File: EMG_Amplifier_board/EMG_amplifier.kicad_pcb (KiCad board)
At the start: 2 copper layers, 50 x 28 mm, 53 parts, among them J1 Conn_01x04_Socket, J2 Conn_01x04_Pin, J3 Conn_01x06_Pin, J4 Conn_01x06_Socket, J7 Conn_01x06_Pin, U1 LPV821DBVR, U2 INA333xxDGK, U3 LPV821DBVR, U5 LPV821DBVR, U6 LPV821DBVR, U7 TPD2E001DRLR, U8 TLV8542DR

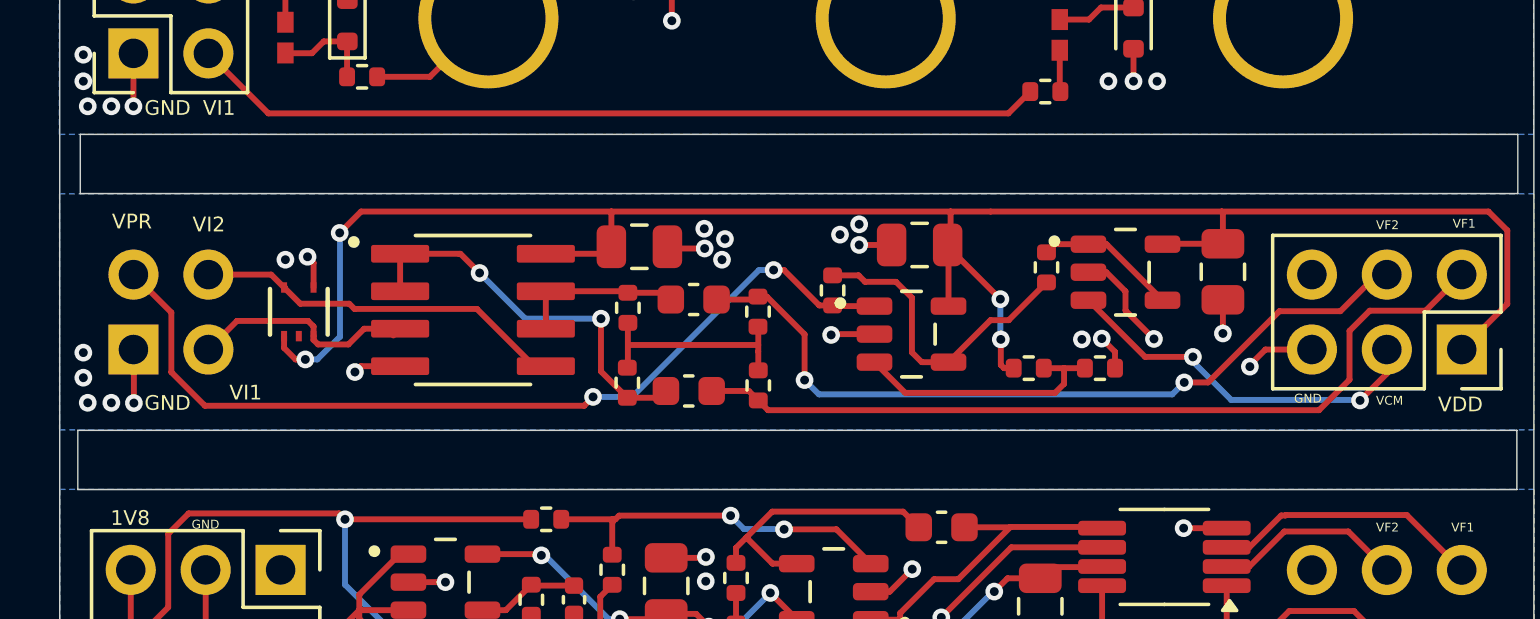
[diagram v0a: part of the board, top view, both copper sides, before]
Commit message: add capacitor to ESD
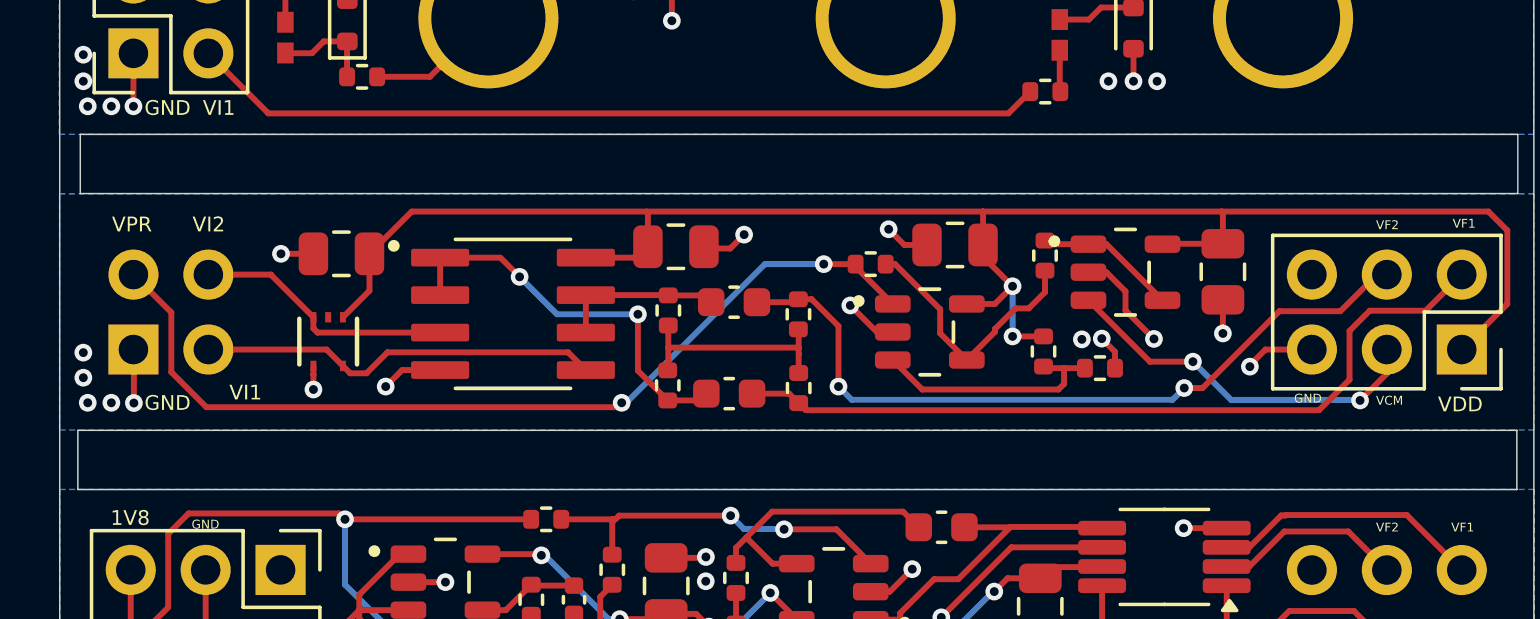
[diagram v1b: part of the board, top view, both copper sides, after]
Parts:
- added C12: 0.1uF, Capacitor_SMD:C_0805_2012Metric, F.Cu at (21.6, 24.1)
- E1: value E1 -> E
- E3: value E2 -> E
- moved R16 1.57 mm to (39.5, 24.4), turned to 180 degrees
- moved U7 1.42 mm to (21.1, 27.0), turned to -90 degrees
- moved R6 1.37 mm to (32.6, 28.5)
- moved R7 1.37 mm to (32.6, 26.0)
- moved C1 1.37 mm to (34.7, 28.8)
- moved C2 1.37 mm to (34.9, 25.7)
- moved R8 1.37 mm to (37.0, 28.6)
- moved R9 1.37 mm to (37.0, 26.1)
- moved U8 1.36 mm to (27.4, 26.1)
- moved C7 1.24 mm to (32.9, 23.8)
- moved C9 1.20 mm to (42.4, 23.8)
- moved R23 0.76 mm to (45.4, 27.4), turned to -90 degrees
- moved U6 0.62 mm to (41.5, 26.7)
- moved R15 0.40 mm to (45.4, 24.1)
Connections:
- J1 pad 2: /Electrode_Board/V_I1 -> /Electrode_Board/V_I2
- J1 pad 4: /Electrode_Board/V_I2 -> /Electrode_Board/V_I1
- J2 pad 2: /Filtering_Board/V_I1 -> /Filtering_Board/V_I2
- J2 pad 4: /Filtering_Board/V_I2 -> /Filtering_Board/V_I1
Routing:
- net /Filtering_Board/+V_DD: track 66.6 -> 60.8 mm, vias 4 -> 2
- net GND: track 40.0 -> 42.2 mm, vias 51 -> 46
- net Net-(U6-IN-): track 10.7 -> 9.15 mm
- net /Filtering_Board/V_F1: track 28.6 -> 27.2 mm
- net /Filtering_Board/V_I2: track 12.7 -> 13.7 mm
- net /Filtering_Board/V_PR: track 30.6 -> 31.4 mm
- net /Filtering_Board/V_F2: track 26.8 -> 25.9 mm
- net /Filtering_Board/V_I1: track 8.17 -> 8.89 mm
- net Net-(U6-IN+): track 8.91 -> 8.26 mm

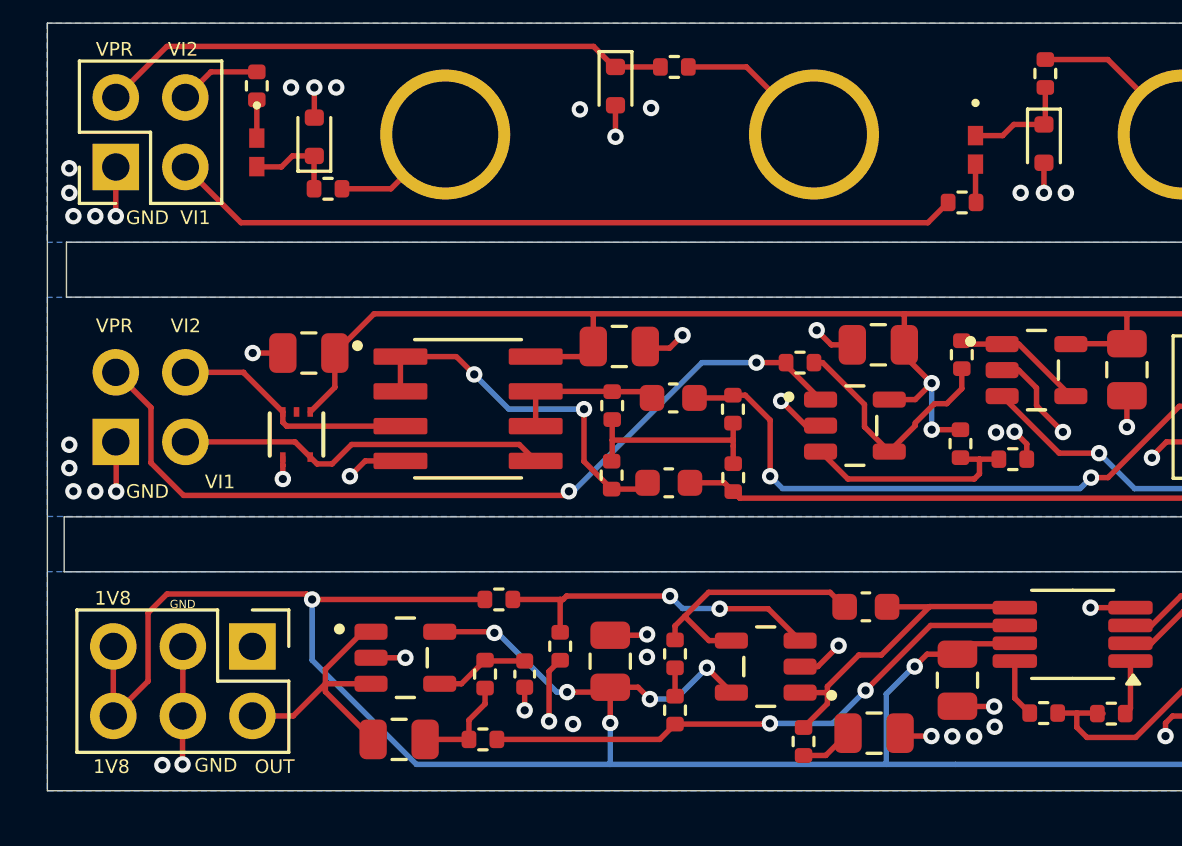
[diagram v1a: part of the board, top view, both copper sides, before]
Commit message: correct the 400Hz LPF schematic and InAmp trace routing
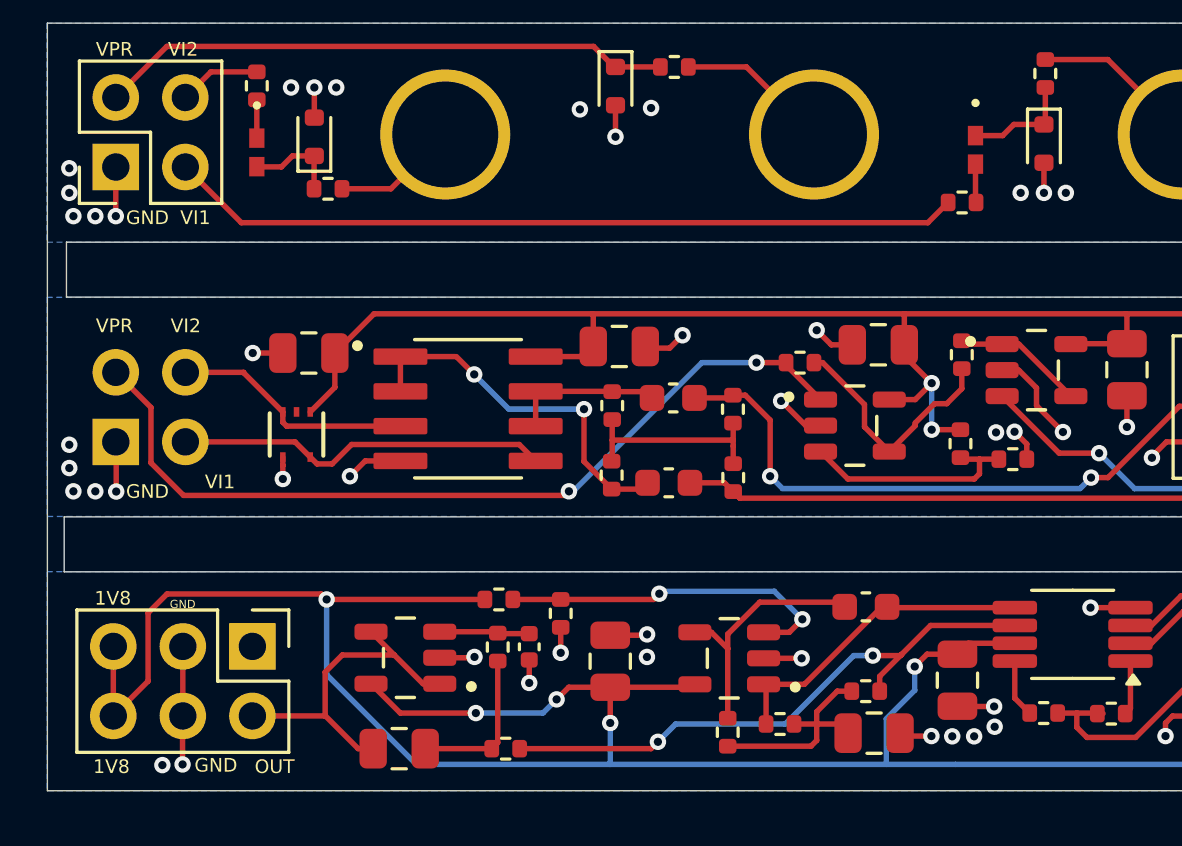
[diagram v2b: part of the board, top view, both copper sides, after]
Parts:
- moved R20 7.00 mm to (41.9, 36.4), turned to 0 degrees
- moved R14 3.45 mm to (36.9, 37.9)
- moved U3 1.37 mm to (36.9, 35.2)
- moved R22 1.20 mm to (30.8, 33.6)
- moved R11 1.09 mm to (28.4, 34.8)
- moved R19 1.07 mm to (38.8, 37.6), turned to 180 degrees
- moved C3 1.01 mm to (29.6, 34.8)
- moved R10 0.90 mm to (28.7, 38.5)
- moved C4 0.34 mm to (24.9, 38.5)
- turned U1 to 180 degrees
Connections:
- C3 pad 1: Net-(U1-IN-) -> Net-(U1-IN+)
- J1 pad 2: /Electrode_Board/V_I2 -> /Electrode_Board/V_I1
- J1 pad 4: /Electrode_Board/V_I1 -> /Electrode_Board/V_I2
- R11 pad 2: Net-(U1-IN-) -> Net-(U1-IN+)
- R14 pad 2: Net-(R14-Pad2) -> Net-(C6-Pad1)
- R20 pad 1: Net-(R14-Pad2) -> Net-(C6-Pad1)
- U1 pad 3: /Processing_Board/V_EMG_OUT -> Net-(U1-IN+)
- U1 pad 4: Net-(U1-IN-) -> /Processing_Board/V_EMG_OUT
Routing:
- net Net-(C6-Pad1): track 1.96 -> 8.11 mm
- net Net-(U1-IN-): track 3.47 -> 0.00 mm
- net Net-(U1-IN+): track 0.00 -> 3.30 mm
- net /Processing_Board/V_EMG_OUT: track 10.3 -> 12.6 mm
- net Net-(C4-Pad1): track 3.72 -> 5.76 mm
- net GND: track 42.2 -> 40.5 mm, vias 46 -> 45
- net Net-(R14-Pad2): track 1.04 -> 0.00 mm
- net /Processing_Board/LPF_400Hz/V_EMG_INA: track 20.6 -> 21.6 mm
- net Net-(U2-Ref): track 12.5 -> 11.9 mm
- net +1V8: track 85.8 -> 85.3 mm, vias 8 -> 6

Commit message: aesthetics
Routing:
- net +1V8: track 85.3 -> 86.1 mm
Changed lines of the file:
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@@
 	)
 	(segment
-		(start 34.35 32.8406)
-		(end 34.1406 33.05)
-		(width 0.2)
-		(layer "F.Cu")
-		(net 30)
-	)
-	(segment
-		(start 34.1406 33.05)
+		(start 34.4 32.8406)
+		(end 34.3906 32.85)
+		(width 0.2)
+		(layer "F.Cu")
+		(net 30)
+	)
+	(segment
+		(start 34.3906 32.85)
+		(end 30.95 32.85)
+		(width 0.2)
+		(layer "F.Cu")
+		(net 30)
+	)
+	(segment
+		(start 30.95 32.85)
 		(end 30.75 33.05)
 		(width 0.2)
@@
 	)
 	(via
-		(at 34.35 32.8406)
-		(size 0.6)
-		(drill 0.3)
-		(layers "F.Cu" "B.Cu")
-		(net 30)
-	)
-	(segment
-		(start 34.4406 32.75)
-		(end 34.35 32.8406)
-		(width 0.2)
-		(layer "B.Cu")
-		(net 30)
-	)
-	(segment
-		(start 39.575 33.775)
-		(end 38.55 32.75)
-		(width 0.2)
-		(layer "B.Cu")
-		(net 30)
-	)
-	(segment
-		(start 38.55 32.75)
-		(end 34.4406 32.75)
+		(at 34.4 32.8406)
+		(size 0.6)
+		(drill 0.3)
+		(layers "F.Cu" "B.Cu")
+		(net 30)
+	)
+	(segment
+		(start 34.4 32.8406)
+		(end 34.4094 32.85)
+		(width 0.2)
+		(layer "B.Cu")
+		(net 30)
+	)
+	(segment
+		(start 34.4094 32.85)
+		(end 38.65 32.85)
+		(width 0.2)
+		(layer "B.Cu")
+		(net 30)
+	)
+	(segment
+		(start 38.65 32.85)
+		(end 39.575 33.775)
 		(width 0.2)
 		(layer "B.Cu")
@@
 	)
 	(segment
+		(start 22.2 35.7964)
+		(end 25.7536 39.35)
+		(width 0.2)
+		(layer "B.Cu")
+		(net 33)
+	)
+	(segment
+		(start 32.8338 39.35)
+		(end 42.9156 39.35)
+		(width 0.2)
+		(layer "B.Cu")
+		(net 33)
+	)
+	(segment
+		(start 42.9156 39.35)
+		(end 57.5352 39.35)
+		(width 0.2)
+		(layer "B.Cu")
+		(net 33)
+	)
+	(segment
+		(start 32.55 39.35)
+		(end 32.5582 39.3418)
+		(width 0.2)
+		(layer "B.Cu")
+		(net 33)
+	)
+	(segment
+		(start 30.1 37.2)
+		(end 30.6 36.7)
+		(width 0.2)
+		(layer "B.Cu")
+		(net 33)
+	)
+	(segment
+		(start 57.5352 39.35)
+		(end 57.8108 39.0744)
+		(width 0.2)
+		(layer "B.Cu")
+		(net 33)
+	)
+	(segment
+		(start 42.7 37.35)
+		(end 43.68 36.37)
+		(width 0.2)
+		(layer "B.Cu")
+		(net 33)
+	)
+	(segment
+		(start 22.2 33.05)
+		(end 22.2 35.7964)
+		(width 0.2)
+		(layer "B.Cu")
+		(net 33)
+	)
+	(segment
+		(start 32.5582 39.3418)
+		(end 32.5582 37.562)
+		(width 0.2)
+		(layer "B.Cu")
+		(net 33)
+	)
+	(segment
+		(start 27.65 37.2)
+		(end 30.1 37.2)
+		(width 0.2)
+		(layer "B.Cu")
+		(net 33)
+	)
+	(segment
 		(start 43.68 36.37)
 		(end 43.68 35.5)
@@
 	)
 	(segment
-		(start 42.64 39.0744)
-		(end 42.64 37.41)
-		(width 0.2)
-		(layer "B.Cu")
-		(net 33)
-	)
-	(segment
-		(start 22.2 33.05)
-		(end 22.2 35.7964)
-		(width 0.2)
-		(layer "B.Cu")
-		(net 33)
-	)
-	(segment
-		(start 32.5582 39.0744)
-		(end 42.64 39.0744)
-		(width 0.2)
-		(layer "B.Cu")
-		(net 33)
-	)
-	(segment
-		(start 25.478 39.0744)
-		(end 32.5582 39.0744)
-		(width 0.2)
-		(layer "B.Cu")
-		(net 33)
-	)
-	(segment
-		(start 30.1 37.2)
-		(end 30.6 36.7)
-		(width 0.2)
-		(layer "B.Cu")
-		(net 33)
-	)
-	(segment
-		(start 42.64 37.41)
-		(end 43.68 36.37)
-		(width 0.2)
-		(layer "B.Cu")
-		(net 33)
-	)
-	(segment
-		(start 42.64 39.0744)
-		(end 45.16 39.0744)
-		(width 0.2)
-		(layer "B.Cu")
-		(net 33)
-	)
-	(segment
-		(start 57.8108 39.0744)
-		(end 45.16 39.0744)
-		(width 0.2)
-		(layer "B.Cu")
-		(net 33)
-	)
-	(segment
-		(start 32.5582 39.0744)
-		(end 32.5582 37.562)
-		(width 0.2)
-		(layer "B.Cu")
-		(net 33)
-	)
-	(segment
-		(start 22.2 35.7964)
-		(end 25.478 39.0744)
-		(width 0.2)
-		(layer "B.Cu")
-		(net 33)
-	)
-	(segment
-		(start 27.65 37.2)
-		(end 30.1 37.2)
-		(width 0.2)
-		(layer "B.Cu")
+		(start 42.7 39.35)
+		(end 42.7 37.35)
+		(width 0.2)
+		(layer "B.Cu")
+		(net 33)
+	)
+	(segment
+		(start 25.7536 39.35)
+		(end 32.8338 39.35)
+		(width 0.2)
+		(layer "B.Cu")

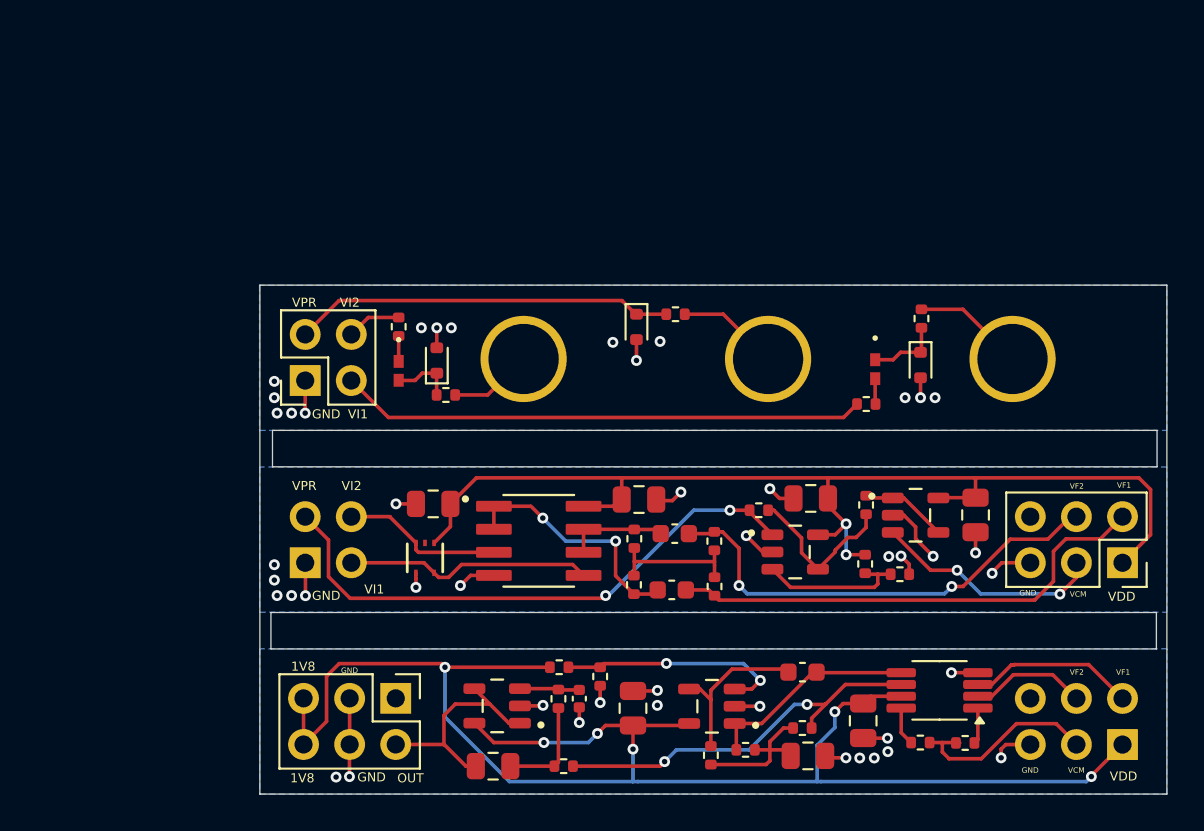
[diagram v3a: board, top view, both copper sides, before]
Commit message: retrace routes that passed under resistances
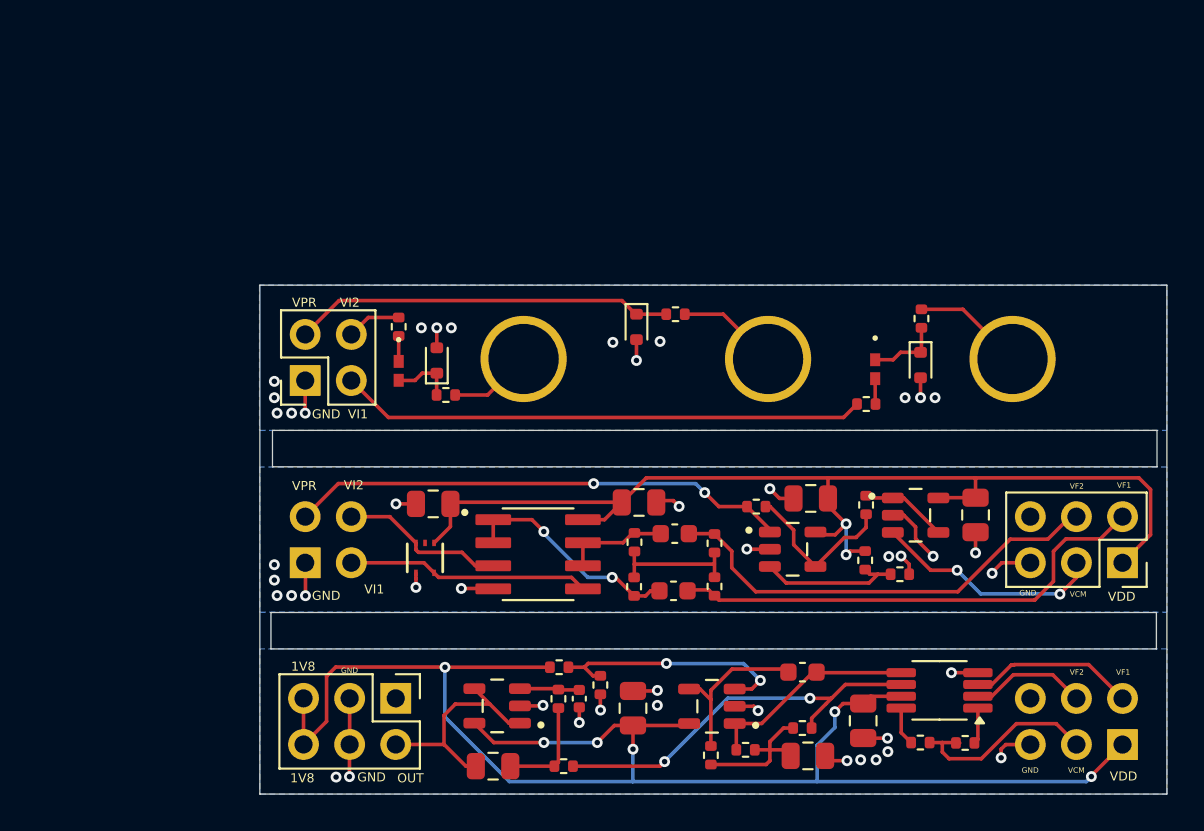
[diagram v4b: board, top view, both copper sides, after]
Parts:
- moved U8 0.74 mm to (27.3, 26.8)
- moved R22 0.47 mm to (30.8, 34.0)
- moved R16 0.24 mm to (39.4, 24.2)
- moved U6 0.21 mm to (41.4, 26.6)
- moved R23 0.20 mm to (45.4, 27.2)
- moved R7 0.19 mm to (32.6, 26.2)
- moved C7 0.16 mm to (32.9, 24.0)
- moved R9 0.12 mm to (37.0, 26.2)
- moved C1 0.11 mm to (34.8, 28.8)
- moved R6 0.10 mm to (32.6, 28.6)
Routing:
- net /Filtering_Board/V_PR: track 31.4 -> 27.6 mm
- net Net-(U8--INA): track 13.5 -> 12.3 mm
- net Net-(U3-IN+): track 12.7 -> 13.7 mm
- net GND: track 40.5 -> 39.5 mm
- net /Filtering_Board/V_F2: track 25.9 -> 25.1 mm, vias 2 -> 0
- net /Filtering_Board/+V_DD: track 60.8 -> 60.0 mm

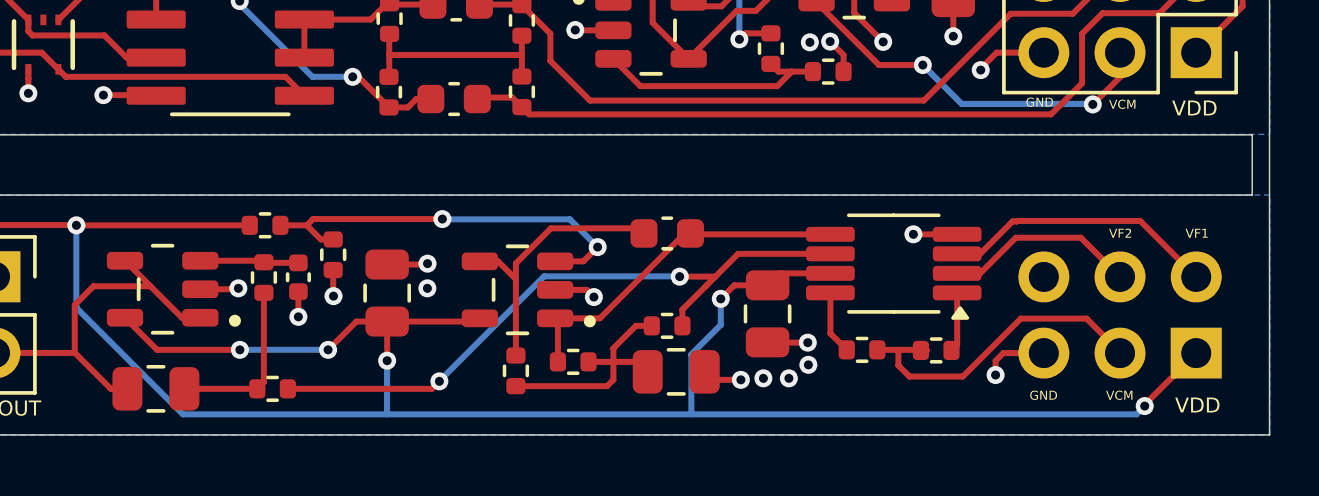
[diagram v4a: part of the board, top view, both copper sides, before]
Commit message: connect InAmp LPV821 to GND
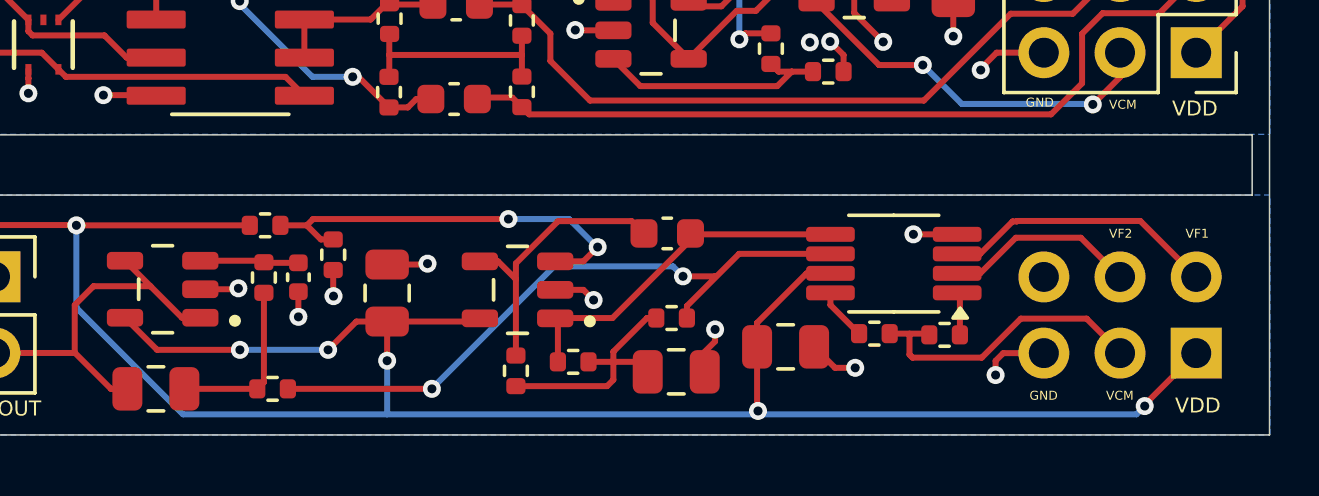
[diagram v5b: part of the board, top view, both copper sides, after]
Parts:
- moved C10 1.25 mm to (45.8, 37.1), turned to 0 degrees
- moved R13 0.68 mm to (48.8, 36.7)
- moved R12 0.59 mm to (51.1, 36.7)
- moved R20 0.30 mm to (42.0, 36.1)
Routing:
- net +1V8: track 85.9 -> 83.8 mm
- net /Processing_Board/V_CM: track 10.8 -> 10.2 mm
- net GND: track 39.5 -> 40.1 mm, vias 45 -> 41
- net Net-(R12-Pad2): track 2.00 -> 1.47 mm
